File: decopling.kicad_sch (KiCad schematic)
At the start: 18 parts

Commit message: Update Mouser prices
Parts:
- C48, C49, C52, C53, C56, C63, C66, C67, C74: Pricing (EUR) 0,11 -> 0,09
- C50, C51, C54, C55, C57, C64, C65, C69, C75: Pricing (EUR) 0,09 -> 0,02
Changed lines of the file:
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@@
       (effects (font (size 1.27 1.27)) hide)
     )
-    (property "Pricing (EUR)" "0,11" (id 7) (at 33.02 34.29 0)
+    (property "Pricing (EUR)" "0,09" (id 7) (at 33.02 34.29 0)
       (effects (font (size 1.27 1.27)) hide)
     )
@@
       (effects (font (size 1.27 1.27)) hide)
     )
-    (property "Pricing (EUR)" "0,09" (id 7) (at 38.1 34.29 0)
+    (property "Pricing (EUR)" "0,02" (id 7) (at 38.1 34.29 0)
       (effects (font (size 1.27 1.27)) hide)
     )
@@
       (effects (font (size 1.27 1.27)) hide)
     )
-    (property "Pricing (EUR)" "0,11" (id 7) (at 54.61 34.29 0)
+    (property "Pricing (EUR)" "0,09" (id 7) (at 54.61 34.29 0)
       (effects (font (size 1.27 1.27)) hide)
     )
@@
       (effects (font (size 1.27 1.27)) hide)
     )
-    (property "Pricing (EUR)" "0,09" (id 7) (at 59.69 34.29 0)
+    (property "Pricing (EUR)" "0,02" (id 7) (at 59.69 34.29 0)
       (effects (font (size 1.27 1.27)) hide)
     )
@@
       (effects (font (size 1.27 1.27)) hide)
     )
-    (property "Pricing (EUR)" "0,11" (id 7) (at 76.2 34.29 0)
+    (property "Pricing (EUR)" "0,09" (id 7) (at 76.2 34.29 0)
       (effects (font (size 1.27 1.27)) hide)
     )
@@
       (effects (font (size 1.27 1.27)) hide)
     )
-    (property "Pricing (EUR)" "0,09" (id 7) (at 81.28 34.29 0)
+    (property "Pricing (EUR)" "0,02" (id 7) (at 81.28 34.29 0)
       (effects (font (size 1.27 1.27)) hide)
     )
@@
       (effects (font (size 1.27 1.27)) hide)
     )
-    (property "Pricing (EUR)" "0,11" (id 7) (at 33.02 67.31 0)
+    (property "Pricing (EUR)" "0,09" (id 7) (at 33.02 67.31 0)
       (effects (font (size 1.27 1.27)) hide)
     )
@@
       (effects (font (size 1.27 1.27)) hide)
     )
-    (property "Pricing (EUR)" "0,09" (id 7) (at 38.1 67.31 0)
+    (property "Pricing (EUR)" "0,02" (id 7) (at 38.1 67.31 0)
       (effects (font (size 1.27 1.27)) hide)
     )
@@
       (effects (font (size 1.27 1.27)) hide)
     )
-    (property "Pricing (EUR)" "0,09" (id 7) (at 124.46 67.31 0)
+    (property "Pricing (EUR)" "0,02" (id 7) (at 124.46 67.31 0)
       (effects (font (size 1.27 1.27)) hide)
     )
@@
       (effects (font (size 1.27 1.27)) hide)
     )
-    (property "Pricing (EUR)" "0,11" (id 7) (at 119.38 67.31 0)
+    (property "Pricing (EUR)" "0,09" (id 7) (at 119.38 67.31 0)
       (effects (font (size 1.27 1.27)) hide)
     )
@@
       (effects (font (size 1.27 1.27)) hide)
     )
-    (property "Pricing (EUR)" "0,11" (id 7) (at 97.79 96.52 0)
+    (property "Pricing (EUR)" "0,09" (id 7) (at 97.79 96.52 0)
       (effects (font (size 1.27 1.27)) hide)
     )
@@
       (effects (font (size 1.27 1.27)) hide)
     )
-    (property "Pricing (EUR)" "0,09" (id 7) (at 102.87 96.52 0)
+    (property "Pricing (EUR)" "0,02" (id 7) (at 102.87 96.52 0)
       (effects (font (size 1.27 1.27)) hide)
     )
@@
       (effects (font (size 1.27 1.27)) hide)
     )
-    (property "Pricing (EUR)" "0,11" (id 7) (at 119.38 96.52 0)
+    (property "Pricing (EUR)" "0,09" (id 7) (at 119.38 96.52 0)
       (effects (font (size 1.27 1.27)) hide)
     )
@@
       (effects (font (size 1.27 1.27)) hide)
     )
-    (property "Pricing (EUR)" "0,09" (id 7) (at 124.46 96.52 0)
+    (property "Pricing (EUR)" "0,02" (id 7) (at 124.46 96.52 0)
       (effects (font (size 1.27 1.27)) hide)
     )
@@
       (effects (font (size 1.27 1.27)) hide)
     )
-    (property "Pricing (EUR)" "0,11" (id 7) (at 142.24 96.52 0)
+    (property "Pricing (EUR)" "0,09" (id 7) (at 142.24 96.52 0)
       (effects (font (size 1.27 1.27)) hide)
     )
@@
       (effects (font (size 1.27 1.27)) hide)
     )
-    (property "Pricing (EUR)" "0,09" (id 7) (at 147.32 96.52 0)
+    (property "Pricing (EUR)" "0,02" (id 7) (at 147.32 96.52 0)
       (effects (font (size 1.27 1.27)) hide)
     )
@@
       (effects (font (size 1.27 1.27)) hide)
     )
-    (property "Pricing (EUR)" "0,11" (id 7) (at 58.42 67.31 0)
+    (property "Pricing (EUR)" "0,09" (id 7) (at 58.42 67.31 0)
       (effects (font (size 1.27 1.27)) hide)
     )
@@
       (effects (font (size 1.27 1.27)) hide)
     )
-    (property "Pricing (EUR)" "0,09" (id 7) (at 63.5 67.31 0)
-      (effects (font (size 1.27 1.27)) hide)
-    )
+    (property "Pricing (EUR)" "0,02" (id 7) (at 63.5 67.31 0)
+      (effects (font (size 1.27 1.27)) hide)
+    )

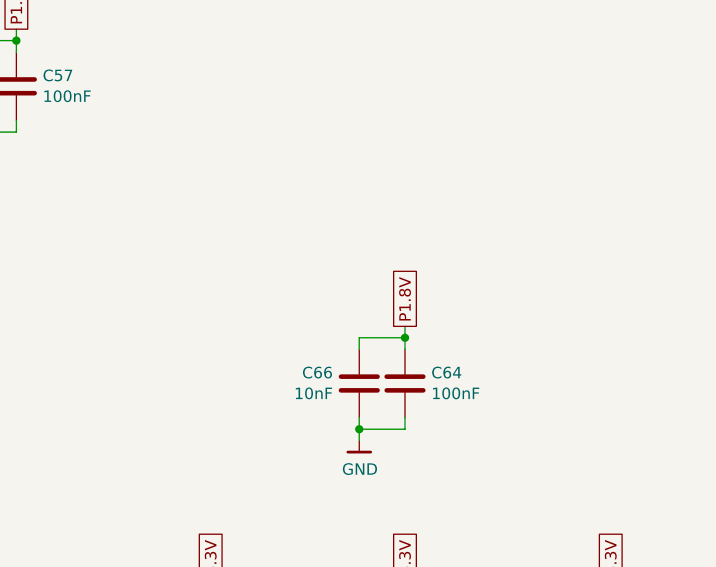
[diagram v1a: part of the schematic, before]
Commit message: Replace HyperRAM with 3V Winbond part
Also remove PSC/PSC# as they are not used on 3V parts.
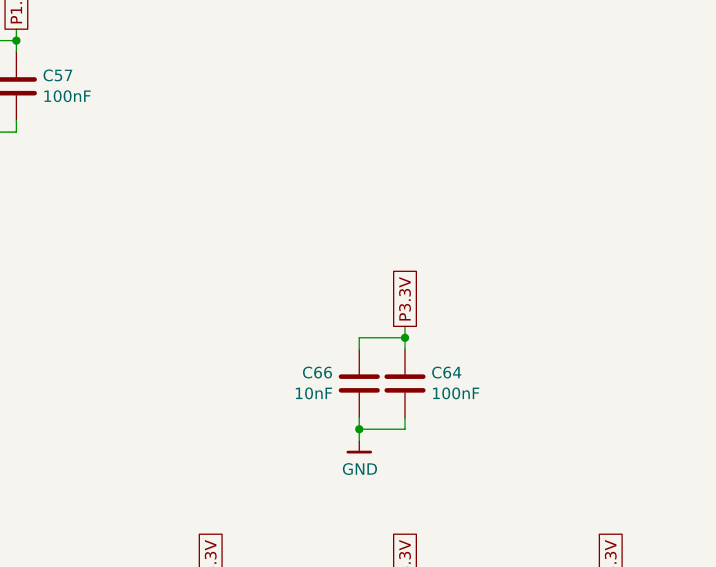
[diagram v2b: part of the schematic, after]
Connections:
- net P1.8V is gone; now on net P3.3V: C64.1, C66.1
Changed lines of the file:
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@@
+    )
+  )
+  (global_label "P3.3V" (shape passive) (at 124.46 60.96 90) (fields_autoplaced)
+    (effects (font (size 1.27 1.27)) (justify left))
+    (property "Intersheet References" "${INTERSHEET_REFS}" (id 0) (at 0 -29.21 0)
+      (effects (font (size 1.27 1.27)) hide)
     )
   )
@@
     (effects (font (size 1.27 1.27)) (justify left))
     (property "Intersheet References" "${INTERSHEET_REFS}" (id 0) (at 0 0 0)
-      (effects (font (size 1.27 1.27)) hide)
-    )
-  )
-  (global_label "P1.8V" (shape passive) (at 124.46 60.96 90) (fields_autoplaced)
-    (effects (font (size 1.27 1.27)) (justify left))
-    (property "Intersheet References" "${INTERSHEET_REFS}" (id 0) (at 0 0 0)

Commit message: Update component prices
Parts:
- C48, C49, C52, C53, C56, C63, C66, C67, C74: Pricing (EUR) 0,09 -> 0,08
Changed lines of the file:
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@@
       (effects (font (size 1.27 1.27)) hide)
     )
-    (property "Pricing (EUR)" "0,09" (at 33.02 34.29 0)
+    (property "Pricing (EUR)" "0,08" (at 33.02 34.29 0)
       (effects (font (size 1.27 1.27)) hide)
     )
@@
       (effects (font (size 1.27 1.27)) hide)
     )
-    (property "Pricing (EUR)" "0,09" (at 54.61 34.29 0)
+    (property "Pricing (EUR)" "0,08" (at 54.61 34.29 0)
       (effects (font (size 1.27 1.27)) hide)
     )
@@
       (effects (font (size 1.27 1.27)) hide)
     )
-    (property "Pricing (EUR)" "0,09" (at 76.2 34.29 0)
+    (property "Pricing (EUR)" "0,08" (at 76.2 34.29 0)
       (effects (font (size 1.27 1.27)) hide)
     )
@@
       (effects (font (size 1.27 1.27)) hide)
     )
-    (property "Pricing (EUR)" "0,09" (at 33.02 67.31 0)
+    (property "Pricing (EUR)" "0,08" (at 33.02 67.31 0)
       (effects (font (size 1.27 1.27)) hide)
     )
@@
       (effects (font (size 1.27 1.27)) hide)
     )
-    (property "Pricing (EUR)" "0,09" (at 119.38 67.31 0)
+    (property "Pricing (EUR)" "0,08" (at 119.38 67.31 0)
       (effects (font (size 1.27 1.27)) hide)
     )
@@
       (effects (font (size 1.27 1.27)) hide)
     )
-    (property "Pricing (EUR)" "0,09" (at 97.79 96.52 0)
+    (property "Pricing (EUR)" "0,08" (at 97.79 96.52 0)
       (effects (font (size 1.27 1.27)) hide)
     )
@@
       (effects (font (size 1.27 1.27)) hide)
     )
-    (property "Pricing (EUR)" "0,09" (at 119.38 96.52 0)
+    (property "Pricing (EUR)" "0,08" (at 119.38 96.52 0)
       (effects (font (size 1.27 1.27)) hide)
     )
@@
       (effects (font (size 1.27 1.27)) hide)
     )
-    (property "Pricing (EUR)" "0,09" (at 142.24 96.52 0)
+    (property "Pricing (EUR)" "0,08" (at 142.24 96.52 0)
       (effects (font (size 1.27 1.27)) hide)
     )
@@
       (effects (font (size 1.27 1.27)) hide)
     )
-    (property "Pricing (EUR)" "0,09" (at 58.42 67.31 0)
-      (effects (font (size 1.27 1.27)) hide)
-    )
+    (property "Pricing (EUR)" "0,08" (at 58.42 67.31 0)
+      (effects (font (size 1.27 1.27)) hide)
+    )
